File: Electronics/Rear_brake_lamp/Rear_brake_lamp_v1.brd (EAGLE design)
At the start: 60.6 x 15.2 mm, 13 parts, among them X1 JST-XH-02-PIN-ROUND-PAD

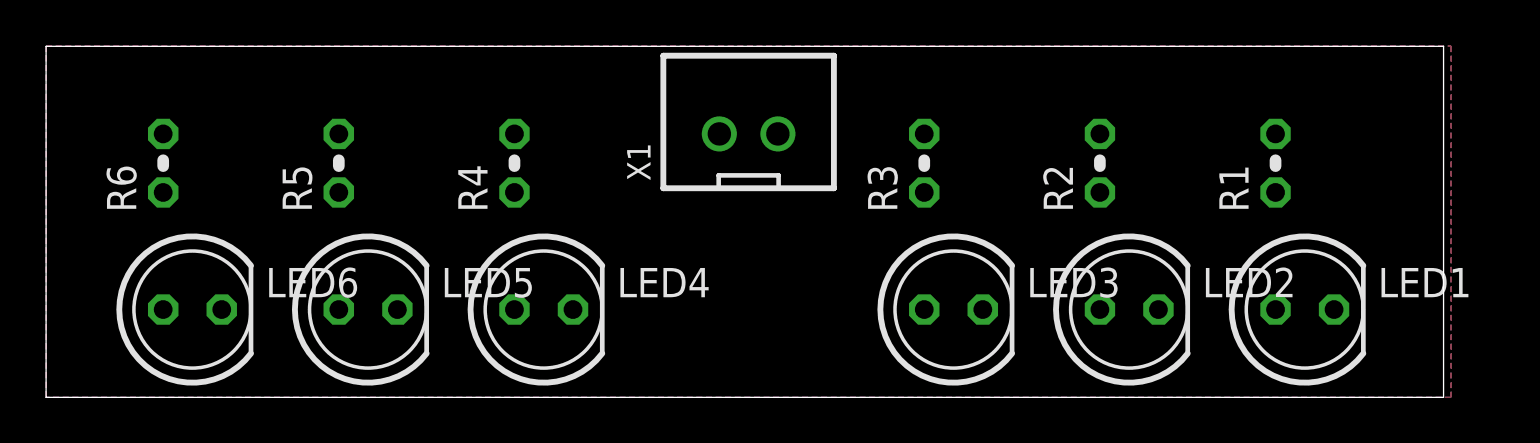
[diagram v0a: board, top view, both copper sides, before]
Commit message: Rear brake lamp done
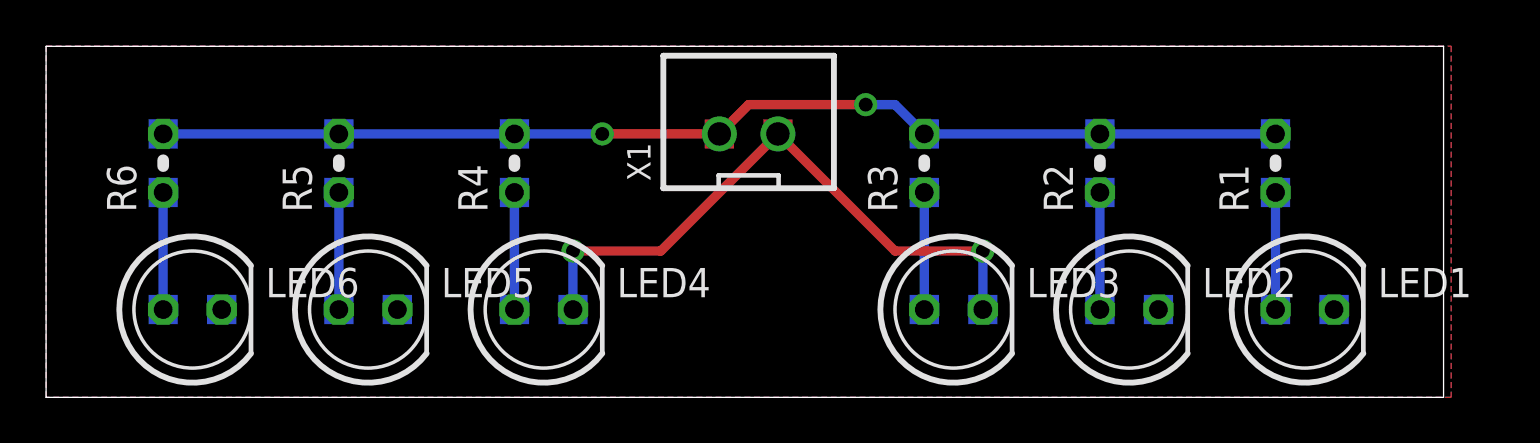
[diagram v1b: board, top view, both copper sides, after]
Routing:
- net API_BRAKE: track 0.00 -> 49.3 mm, vias 0 -> 2
- net GND: track 0.00 -> 27.1 mm, vias 0 -> 2
- net N$6: track 0.00 -> 5.08 mm
- net N$5: track 0.00 -> 5.08 mm
- net N$4: track 0.00 -> 5.08 mm
- net N$3: track 0.00 -> 5.08 mm
- net N$2: track 0.00 -> 5.08 mm
- net N$1: track 0.00 -> 5.08 mm
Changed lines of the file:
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@@
 <layer number="43" name="vRestrict" color="2" fill="10" visible="yes" active="yes"/>
 <layer number="44" name="Drills" color="7" fill="1" visible="no" active="yes"/>
-<layer number="45" name="Holes" color="7" fill="1" visible="no" active="yes"/>
+<layer number="45" name="Holes" color="7" fill="1" visible="yes" active="yes"/>
 <layer number="46" name="Milling" color="3" fill="1" visible="no" active="yes"/>
 <layer number="47" name="Measures" color="7" fill="1" visible="no" active="yes"/>
@@
 <dimension x1="6.35" y1="3.81" x2="6.35" y2="0" x3="-7.62" y3="1.905" textsize="1.778" layer="20"/>
 <dimension x1="30.48" y1="11.43" x2="30.48" y2="0" x3="-11.43" y3="5.715" textsize="1.778" layer="20"/>
+<rectangle x1="4.445" y1="8.255" x2="5.715" y2="9.525" layer="16"/>
+<rectangle x1="4.445" y1="10.795" x2="5.715" y2="12.065" layer="16"/>
+<rectangle x1="12.065" y1="10.795" x2="13.335" y2="12.065" layer="16"/>
+<rectangle x1="12.065" y1="8.255" x2="13.335" y2="9.525" layer="16"/>
+<rectangle x1="19.685" y1="10.795" x2="20.955" y2="12.065" layer="16"/>
+<rectangle x1="19.685" y1="8.255" x2="20.955" y2="9.525" layer="16"/>
+<rectangle x1="4.445" y1="3.175" x2="5.715" y2="4.445" layer="16"/>
+<rectangle x1="6.985" y1="3.175" x2="8.255" y2="4.445" layer="16"/>
+<rectangle x1="12.065" y1="3.175" x2="13.335" y2="4.445" layer="16"/>
+<rectangle x1="14.605" y1="3.175" x2="15.875" y2="4.445" layer="16"/>
+<rectangle x1="19.685" y1="3.175" x2="20.955" y2="4.445" layer="16"/>
+<rectangle x1="22.225" y1="3.175" x2="23.495" y2="4.445" layer="16"/>
+<rectangle x1="37.465" y1="10.795" x2="38.735" y2="12.065" layer="16"/>
+<rectangle x1="37.465" y1="8.255" x2="38.735" y2="9.525" layer="16"/>
+<rectangle x1="45.085" y1="10.795" x2="46.355" y2="12.065" layer="16"/>
+<rectangle x1="45.085" y1="8.255" x2="46.355" y2="9.525" layer="16"/>
+<rectangle x1="52.705" y1="10.795" x2="53.975" y2="12.065" layer="16"/>
+<rectangle x1="52.705" y1="8.255" x2="53.975" y2="9.525" layer="16"/>
+<rectangle x1="37.465" y1="3.175" x2="38.735" y2="4.445" layer="16"/>
+<rectangle x1="40.005" y1="3.175" x2="41.275" y2="4.445" layer="16"/>
+<rectangle x1="45.085" y1="3.175" x2="46.355" y2="4.445" layer="16"/>
+<rectangle x1="47.625" y1="3.175" x2="48.895" y2="4.445" layer="16"/>
+<rectangle x1="52.705" y1="3.175" x2="53.975" y2="4.445" layer="16"/>
+<rectangle x1="55.245" y1="3.175" x2="56.515" y2="4.445" layer="16"/>
+<rectangle x1="28.575" y1="10.795" x2="29.845" y2="12.065" layer="1"/>
+<rectangle x1="31.115" y1="10.795" x2="32.385" y2="12.065" layer="1"/>
 </plain>
 <attributes>
@@
 <contactref element="R1" pad="1"/>
 <contactref element="LED1" pad="A"/>
-<wire x1="53.34" y1="3.81" x2="53.34" y2="8.89" width="0" layer="19" extent="1-1"/>
+<wire x1="53.34" y1="8.89" x2="53.34" y2="3.81" width="0.4064" layer="16"/>
 </signal>
 <signal name="N$2">
 <contactref element="R2" pad="1"/>
 <contactref element="LED2" pad="A"/>
-<wire x1="45.72" y1="8.89" x2="45.72" y2="3.81" width="0" layer="19" extent="1-1"/>
+<wire x1="45.72" y1="8.89" x2="45.72" y2="3.81" width="0.4064" layer="16"/>
 </signal>
 <signal name="N$3">
 <contactref element="R3" pad="1"/>
 <contactref element="LED3" pad="A"/>
-<wire x1="38.1" y1="3.81" x2="38.1" y2="8.89" width="0" layer="19" extent="1-1"/>
+<wire x1="38.1" y1="8.89" x2="38.1" y2="3.81" width="0.4064" layer="16"/>
 </signal>
 <signal name="API_BRAKE">
@@
 <contactref element="R5" pad="2"/>
 <contactref element="R6" pad="2"/>
-<wire x1="53.34" y1="11.43" x2="5.08" y2="11.43" width="0" layer="19" extent="1-1"/>
-<wire x1="45.72" y1="11.43" x2="53.34" y2="11.43" width="0" layer="19" extent="1-1"/>
-<wire x1="38.1" y1="11.43" x2="45.72" y2="11.43" width="0" layer="19" extent="1-1"/>
-<wire x1="20.32" y1="11.43" x2="38.1" y2="11.43" width="0" layer="19" extent="1-1"/>
-<wire x1="12.7" y1="11.43" x2="20.32" y2="11.43" width="0" layer="19" extent="1-1"/>
-<wire x1="29.21" y1="11.43" x2="20.32" y2="11.43" width="0" layer="19" extent="1-1"/>
+<wire x1="29.21" y1="11.43" x2="24.13" y2="11.43" width="0.4064" layer="1"/>
+<via x="24.13" y="11.43" extent="1-16" drill="0.6" shape="octagon"/>
+<wire x1="24.13" y1="11.43" x2="20.32" y2="11.43" width="0.4064" layer="16"/>
+<wire x1="20.32" y1="11.43" x2="12.7" y2="11.43" width="0.4064" layer="16"/>
+<wire x1="12.7" y1="11.43" x2="5.08" y2="11.43" width="0.4064" layer="16"/>
+<wire x1="29.21" y1="11.43" x2="30.48" y2="12.7" width="0.4064" layer="1"/>
+<wire x1="30.48" y1="12.7" x2="35.56" y2="12.7" width="0.4064" layer="1"/>
+<via x="35.56" y="12.7" extent="1-16" drill="0.6" shape="octagon"/>
+<wire x1="35.56" y1="12.7" x2="36.83" y2="12.7" width="0.4064" layer="16"/>
+<wire x1="36.83" y1="12.7" x2="38.1" y2="11.43" width="0.4064" layer="16"/>
+<wire x1="38.1" y1="11.43" x2="45.72" y2="11.43" width="0.4064" layer="16"/>
+<wire x1="45.72" y1="11.43" x2="53.34" y2="11.43" width="0.4064" layer="16"/>
 </signal>
 <signal name="GND">
@@
 <contactref element="LED4" pad="K"/>
 <contactref element="X1" pad="2"/>
-<wire x1="48.26" y1="3.81" x2="31.75" y2="11.43" width="0" layer="19" extent="1-1"/>
-<wire x1="22.86" y1="3.81" x2="48.26" y2="3.81" width="0" layer="19" extent="1-1"/>
-<wire x1="7.62" y1="3.81" x2="22.86" y2="3.81" width="0" layer="19" extent="1-1"/>
-<wire x1="55.88" y1="3.81" x2="31.75" y2="11.43" width="0" layer="19" extent="1-1"/>
-<wire x1="40.64" y1="3.81" x2="55.88" y2="3.81" width="0" layer="19" extent="1-1"/>
-<wire x1="15.24" y1="3.81" x2="40.64" y2="3.81" width="0" layer="19" extent="1-1"/>
 <polygon width="0.4064" layer="1">
 <vertex x="0" y="15.24"/>
@@
 <vertex x="0" y="0"/>
 </polygon>
+<wire x1="22.86" y1="3.81" x2="22.86" y2="6.35" width="0.4064" layer="16"/>
+<via x="22.86" y="6.35" extent="1-16" drill="0.6" shape="octagon"/>
+<wire x1="22.86" y1="6.35" x2="26.67" y2="6.35" width="0.4064" layer="1"/>
+<wire x1="26.67" y1="6.35" x2="31.75" y2="11.43" width="0.4064" layer="1"/>
+<wire x1="40.64" y1="3.81" x2="40.64" y2="6.35" width="0.4064" layer="16"/>
+<via x="40.64" y="6.35" extent="1-16" drill="0.6" shape="octagon"/>
+<wire x1="40.64" y1="6.35" x2="36.83" y2="6.35" width="0.4064" layer="1"/>
+<wire x1="36.83" y1="6.35" x2="31.75" y2="11.43" width="0.4064" layer="1"/>
 </signal>
 <signal name="N$4">
 <contactref element="R4" pad="1"/>
 <contactref element="LED4" pad="A"/>
-<wire x1="20.32" y1="8.89" x2="20.32" y2="3.81" width="0" layer="19" extent="1-1"/>
+<wire x1="20.32" y1="8.89" x2="20.32" y2="3.81" width="0.4064" layer="16"/>
 </signal>
 <signal name="N$5">
 <contactref element="R5" pad="1"/>
 <contactref element="LED5" pad="A"/>
-<wire x1="12.7" y1="8.89" x2="12.7" y2="3.81" width="0" layer="19" extent="1-1"/>
+<wire x1="12.7" y1="8.89" x2="12.7" y2="3.81" width="0.4064" layer="16"/>
 </signal>
 <signal name="N$6">
 <contactref element="R6" pad="1"/>
 <contactref element="LED6" pad="A"/>
-<wire x1="5.08" y1="3.81" x2="5.08" y2="8.89" width="0" layer="19" extent="1-1"/>
+<wire x1="5.08" y1="8.89" x2="5.08" y2="3.81" width="0.4064" layer="16"/>
 </signal>
 </signals>
